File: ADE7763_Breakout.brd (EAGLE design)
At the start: 32.7 x 26.7 mm, 24 parts, among them J1 10p-2.54, Q1 3.58MHz, U1 ADE7763ARSZ

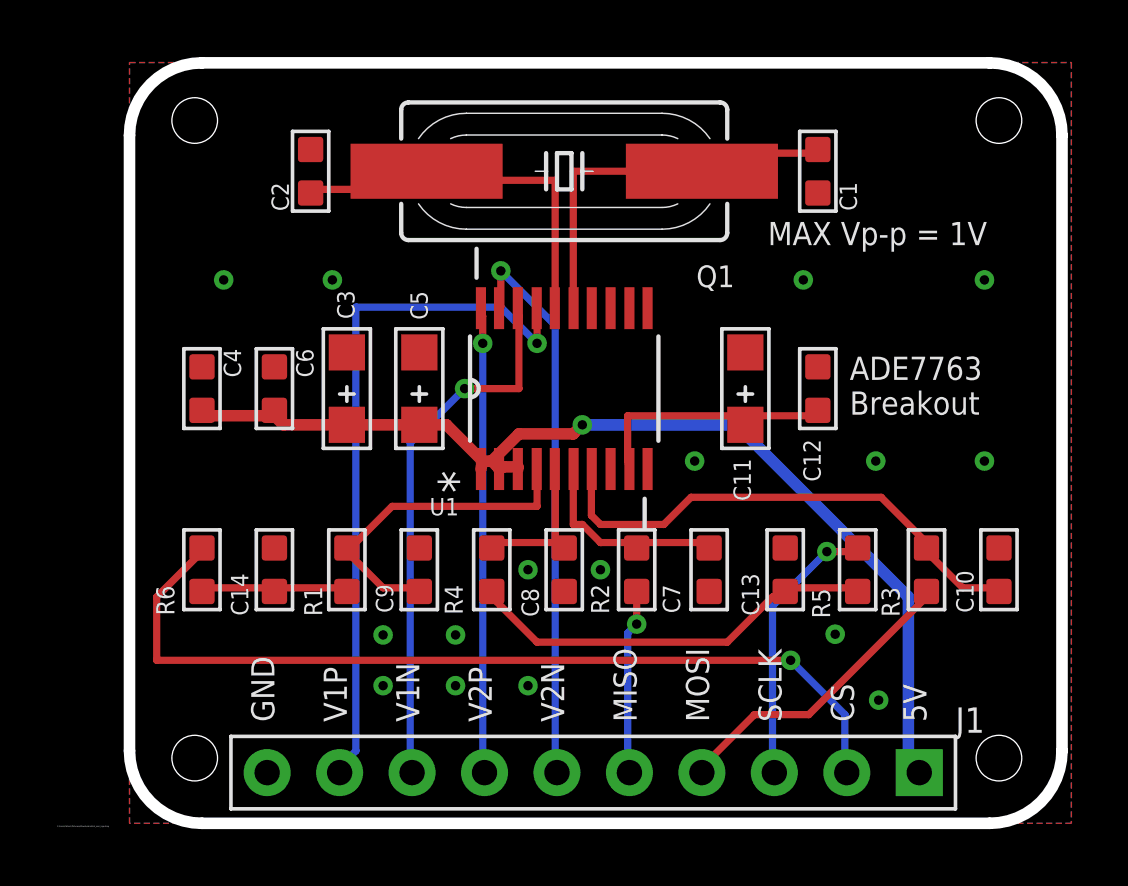
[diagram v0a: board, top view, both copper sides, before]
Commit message: Corrected footprint and labels, added wirepads for other pins
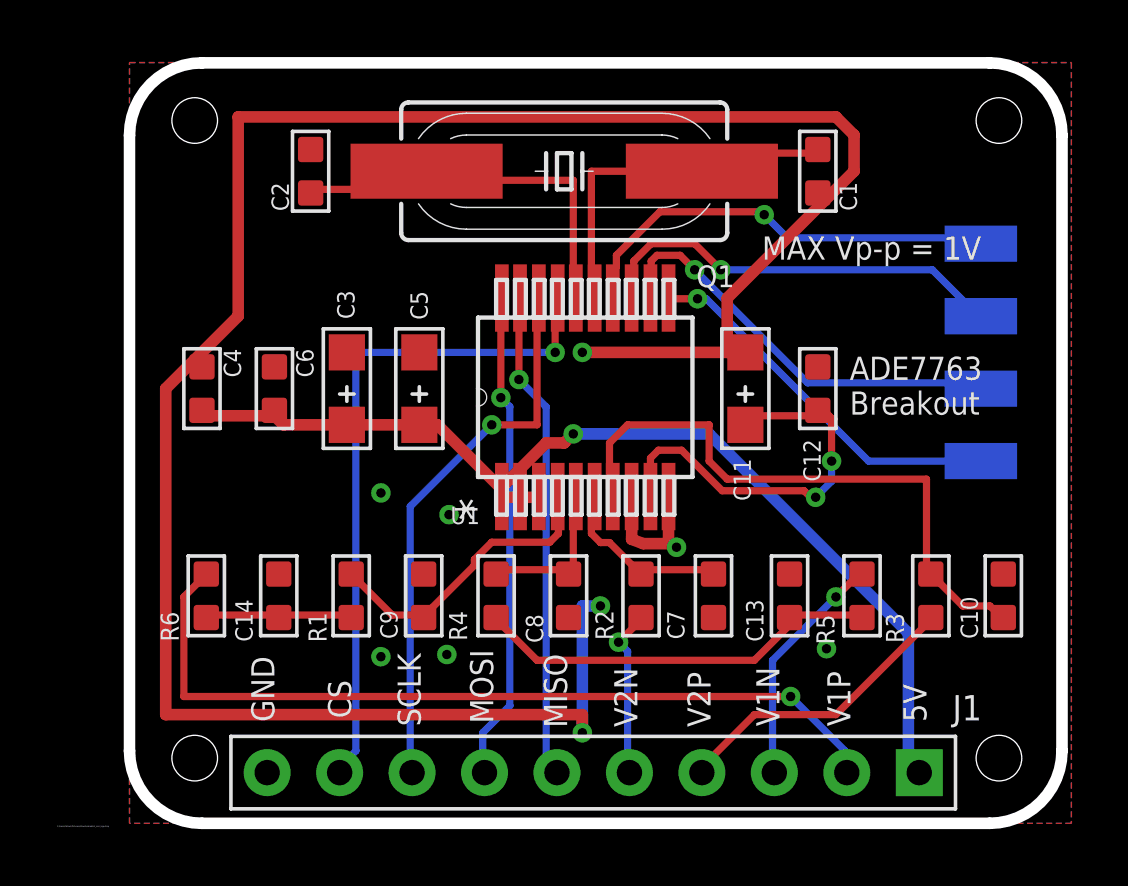
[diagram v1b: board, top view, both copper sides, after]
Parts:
- added CF, INT, SAG, ZX: WIREPADSMD1,27-254, wirepad:SMD1,27-2,54
- U1: value ADE7763ARSZ -> ADE7763ARSZSSOP20; device Analog Devices_By_element14_Batch_1:SOP65P640X120-20N -> Analog Devices_By_element14_Batch_1:RS_20-M
- moved C10 0.93 mm to (33.2, 7.98)
- moved C13 0.93 mm to (25.7, 7.98)
- moved C14 0.93 mm to (7.77, 7.98)
- moved C7 0.93 mm to (23.0, 7.98)
- moved C8 0.93 mm to (17.9, 7.98)
- moved C9 0.93 mm to (12.9, 7.98)
- moved R1 0.93 mm to (10.3, 7.98)
- moved R2 0.93 mm to (20.5, 7.98)
- moved R3 0.93 mm to (30.6, 7.98)
- moved R4 0.93 mm to (15.4, 7.98)
- moved R5 0.93 mm to (28.2, 7.98)
- moved R6 0.93 mm to (5.23, 7.98)
- moved U1 0.80 mm to (18.5, 14.9)
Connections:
- new net N$10: U1.12, ZX.1
- new net N$11: CF.1, U1.11
- new net N$3: INT.1, U1.14
- new net N$8: SAG.1, U1.13
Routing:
- net AGND: track 0.00 -> 83.5 mm, vias 16 -> 9
- net N$3: track 0.00 -> 15.4 mm, vias 0 -> 1
- net N$10: track 0.00 -> 14.9 mm, vias 0 -> 1
- net N$8: track 0.00 -> 14.8 mm, vias 0 -> 1
- net N$11: track 0.00 -> 13.3 mm, vias 0 -> 1
- net N$9: track 9.18 -> 14.7 mm, vias 0 -> 2
- net N$6: track 18.1 -> 21.4 mm
- net MISO: track 19.7 -> 17.2 mm
- net V1P: track 31.6 -> 29.4 mm
- net N$7: track 12.0 -> 10.5 mm
- net V1N: track 9.68 -> 8.32 mm
- net N$4: track 7.35 -> 6.38 mm
- net MOSI: track 16.3 -> 17.2 mm
- net CLKIN: track 13.8 -> 12.9 mm
- net CS: track 24.7 -> 24.0 mm
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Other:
- board text added: "v1.0 25/11/2015"
- board text removed: "v1.0 27/10/2015"
